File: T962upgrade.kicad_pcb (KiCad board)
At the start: 2 copper layers, 63.5 x 63.5 mm, 92 parts, among them J1 K Type, J10 UART, J2 USB_B_Micro, J3 USB_X, J4 K Type, J5 K Type, J6 K Type, J7 Fan In, J8 Fan Out, J9 K Type, Q1 2N7002, Q2 2N7002, SW1 Boot, SW2 Boot, U1 MAX31850KATB, U2 CH340C, U3 LM317_3PinPackage, U4 LM317_3PinPackage, U5 MAX31850KATB, U6 MAX31850KATB, U7 MAX31850KATB, U8 DS18S20, U9 TMP709

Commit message: Updated gerber
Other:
- board text added: "JLCJLCJLCJLC"
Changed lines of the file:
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@@
   (general
     (thickness 1.6)
-    (drawings 40)
+    (drawings 41)
     (tracks 585)
     (zones 0)
@@
     (pcbplotparams
       (layerselection 0x010f8_ffffffff)
-      (usegerberextensions false)
+      (usegerberextensions true)
       (usegerberattributes false)
       (usegerberadvancedattributes false)
@@
       (plotinvisibletext false)
       (padsonsilk false)
-      (subtractmaskfromsilk false)
+      (subtractmaskfromsilk true)
       (outputformat 1)
       (mirror false)
@@
     )
   )
+  (gr_text JLCJLCJLCJLC (at 88.265 64.77) (layer F.SilkS)
+    (effects (font (size 0.8 0.8) (thickness 0.15)))
+  )
   (gr_text "T-962/T-962A upgrade" (at 74.295 73.025) (layer F.SilkS)

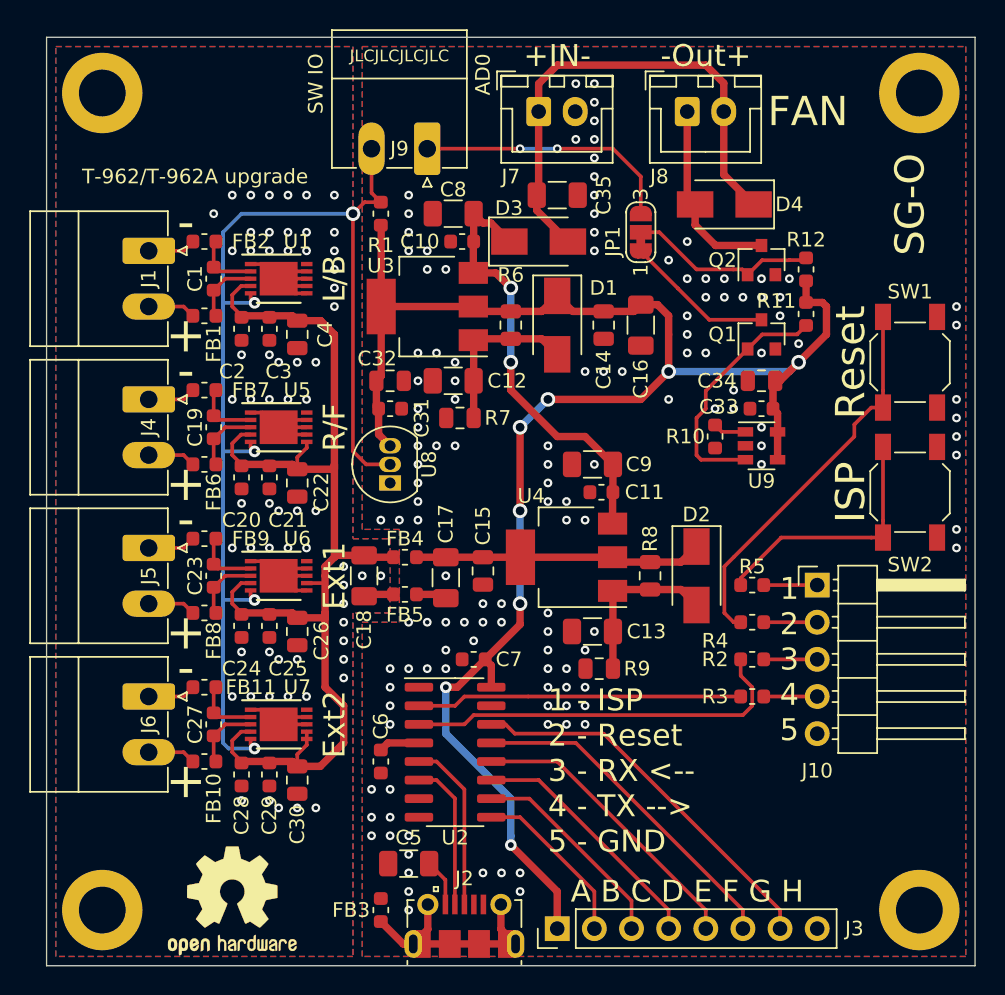
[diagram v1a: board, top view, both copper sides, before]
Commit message: Added optional through hole resistor to set fan switch on temperature.
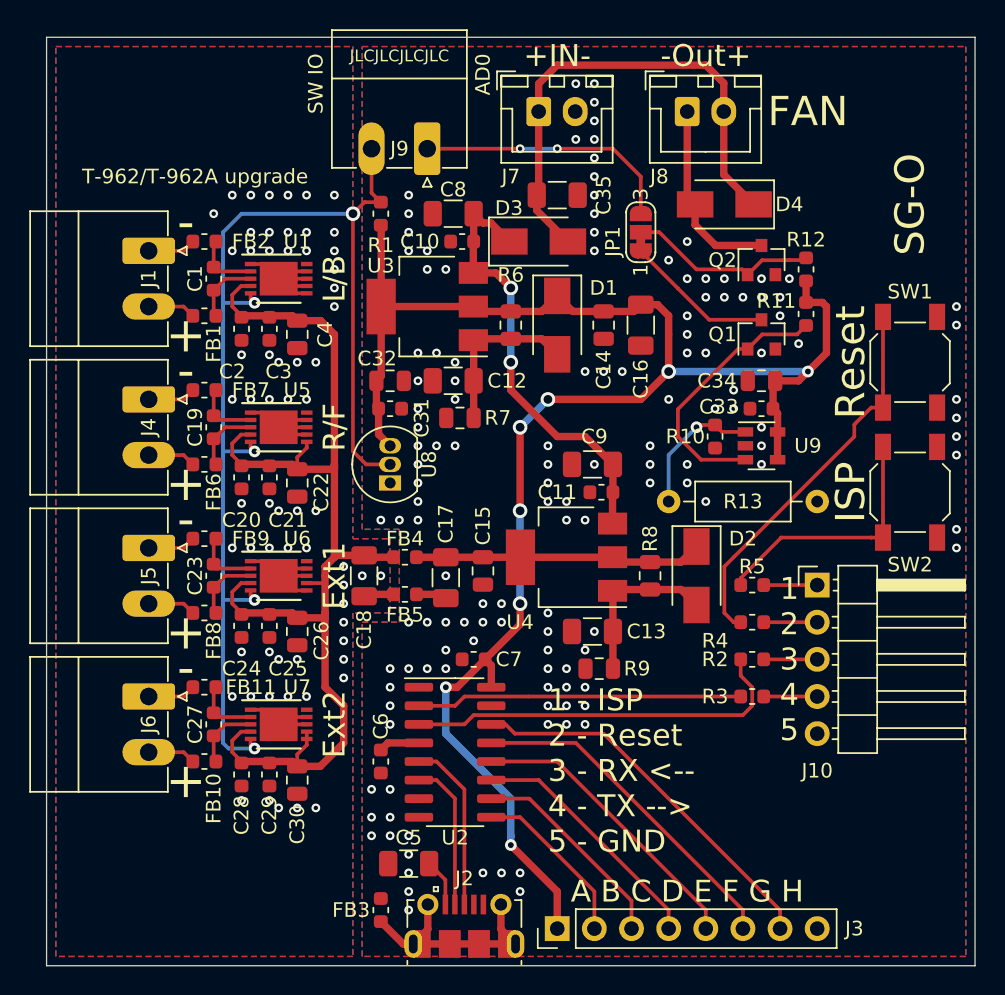
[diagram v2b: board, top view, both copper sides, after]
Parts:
- removed REF**: OSHW-Logo2_9.8x8mm_Copper, Symbol:OSHW-Logo2_9.8x8mm_Copper
- removed REF**: OSHW-Logo2_9.8x8mm_SilkScreen, Symbol:OSHW-Logo2_9.8x8mm_SilkScreen
- removed REF** (x4): MountingHole_3.2mm_M3_ISO14580_Pad, MountingHole:MountingHole_3.2mm_M3_ISO14580_Pad
- added R13: DNP, Resistor_THT:R_Axial_DIN0207_L6.3mm_D2.5mm_P10.16mm_Horizontal, F.Cu at (106.7, 95.2)
- R10: value 52k3 -> 62k
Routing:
- net Net-(R10-Pad1): track 2.27 -> 9.47 mm, vias 0 -> 1
- net VDD: track 118.9 -> 120.3 mm
- net Net-(Q1-Pad1): track 16.8 -> 18.3 mm
- net VSS: vias 130 -> 136
